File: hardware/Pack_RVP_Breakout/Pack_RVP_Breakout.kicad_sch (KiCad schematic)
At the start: 4 parts, among them Q1 Q_PMOS_GDS, Q2 Q_PMOS_GDS

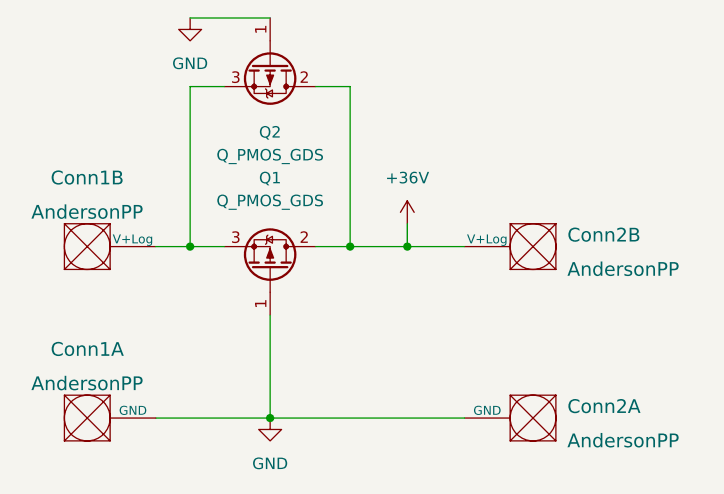
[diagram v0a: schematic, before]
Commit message: Made 30V version
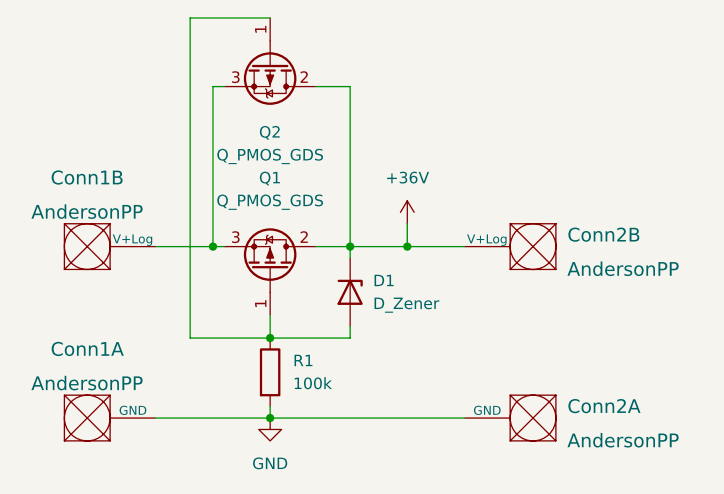
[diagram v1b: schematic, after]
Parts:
- added D1: D_Zener, MRDT_Passives:SOT-23_Diode, symbol Device:D_Zener
- added R1: 100k, Resistor_SMD:R_0603_1608Metric_Pad0.98x0.95mm_HandSolder, symbol Device:R
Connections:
- net +36V: now also D1.1 (K)
- net GND: now also R1.2; no longer Q1.1 (G), Q2.1 (G)
- new net: D1.2 (A), Q1.1 (G), Q2.1 (G), R1.1
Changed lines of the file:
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@@
   (junction (at 106.68 69.85) (diameter 0) (color 0 0 0 0)
   )
+  (junction (at 85.09 69.85) (diameter 0) (color 0 0 0 0)
+  )
   (junction (at 91.44 88.9) (diameter 0) (color 0 0 0 0)
   )
-  (junction (at 82.55 69.85) (diameter 0) (color 0 0 0 0)
-  )
   (junction (at 100.33 69.85) (diameter 0) (color 0 0 0 0)
   )
-  (wire (pts (xy 86.36 52.07) (xy 82.55 52.07))
+  (junction (at 91.44 80.01) (diameter 0) (color 0 0 0 0)
+  )
+  (wire (pts (xy 86.36 52.07) (xy 85.09 52.07))
+    (stroke (width 0) (type default) (color 0 0 0 0))
+  )
+  (wire (pts (xy 82.55 44.45) (xy 82.55 80.01))
     (stroke (width 0) (type default) (color 0 0 0 0))
   )
@@
     (stroke (width 0) (type default) (color 0 0 0 0))
   )
-  (wire (pts (xy 82.55 52.07) (xy 82.55 69.85))
-    (stroke (width 0) (type default) (color 0 0 0 0))
-  )
   (wire (pts (xy 78.74 88.9) (xy 91.44 88.9))
     (stroke (width 0) (type default) (color 0 0 0 0))
   )
+  (wire (pts (xy 85.09 52.07) (xy 85.09 69.85))
+    (stroke (width 0) (type default) (color 0 0 0 0))
+  )
   (wire (pts (xy 82.55 44.45) (xy 91.44 44.45))
     (stroke (width 0) (type default) (color 0 0 0 0))
   )
+  (wire (pts (xy 100.33 78.74) (xy 100.33 80.01))
+    (stroke (width 0) (type default) (color 0 0 0 0))
+  )
+  (wire (pts (xy 82.55 80.01) (xy 91.44 80.01))
+    (stroke (width 0) (type default) (color 0 0 0 0))
+  )
+  (wire (pts (xy 100.33 69.85) (xy 100.33 71.12))
+    (stroke (width 0) (type default) (color 0 0 0 0))
+  )
   (wire (pts (xy 106.68 69.85) (xy 113.03 69.85))
     (stroke (width 0) (type default) (color 0 0 0 0))
   )
-  (wire (pts (xy 82.55 69.85) (xy 86.36 69.85))
-    (stroke (width 0) (type default) (color 0 0 0 0))
-  )
-  (wire (pts (xy 78.74 69.85) (xy 82.55 69.85))
+  (wire (pts (xy 91.44 87.63) (xy 91.44 88.9))
+    (stroke (width 0) (type default) (color 0 0 0 0))
+  )
+  (wire (pts (xy 78.74 69.85) (xy 85.09 69.85))
     (stroke (width 0) (type default) (color 0 0 0 0))
   )
@@
     (stroke (width 0) (type default) (color 0 0 0 0))
   )
+  (wire (pts (xy 100.33 80.01) (xy 91.44 80.01))
+    (stroke (width 0) (type default) (color 0 0 0 0))
+  )
+  (wire (pts (xy 85.09 69.85) (xy 86.36 69.85))
+    (stroke (width 0) (type default) (color 0 0 0 0))
+  )
   (wire (pts (xy 96.52 69.85) (xy 100.33 69.85))
     (stroke (width 0) (type default) (color 0 0 0 0))
   )
-  (wire (pts (xy 91.44 77.47) (xy 91.44 88.9))
+  (wire (pts (xy 91.44 77.47) (xy 91.44 80.01))
     (stroke (width 0) (type default) (color 0 0 0 0))
   )
@@
     (stroke (width 0) (type default) (color 0 0 0 0))
   )
+  (symbol (lib_id "Device:R") (at 91.44 83.82 0) (unit 1)
+    (in_bom yes) (on_board yes) (fields_autoplaced)
+    (property "Reference" "R1" (id 0) (at 93.98 82.5499 0)
+      (effects (font (size 1.27 1.27)) (justify left))
+    )
+    (property "Value" "100k" (id 1) (at 93.98 85.0899 0)
+      (effects (font (size 1.27 1.27)) (justify left))
+    )
+    (property "Footprint" "Resistor_SMD:R_0603_1608Metric_Pad0.98x0.95mm_HandSolder" (id 2) (at 89.662 83.82 90)
+      (effects (font (size 1.27 1.27)) hide)
+    )
+    (property "Datasheet" "~" (id 3) (at 91.44 83.82 0)
+      (effects (font (size 1.27 1.27)) hide)
+    )
+    (pin "1")
+    (pin "2")
+  )
   (symbol (lib_id "power:+36V") (at 106.68 67.31 0) (unit 1)
     (in_bom yes) (on_board yes) (fields_autoplaced)
-    (property "Reference" "#PWR?" (id 0) (at 106.68 71.12 0)
+    (property "Reference" "#PWR03" (id 0) (at 106.68 71.12 0)
       (effects (font (size 1.27 1.27)) hide)
     )
@@
     )
     (pin "1")
+  )
+  (symbol (lib_id "Device:D_Zener") (at 100.33 74.93 270) (unit 1)
+    (in_bom yes) (on_board yes) (fields_autoplaced)
+    (property "Reference" "D1" (id 0) (at 102.87 73.6599 90)
+      (effects (font (size 1.27 1.27)) (justify left))
+    )
+    (property "Value" "D_Zener" (id 1) (at 102.87 76.1999 90)
+      (effects (font (size 1.27 1.27)) (justify left))
+    )
+    (property "Footprint" "MRDT_Passives:SOT-23_Diode" (id 2) (at 100.33 74.93 0)
+      (effects (font (size 1.27 1.27)) hide)
+    )
+    (property "Datasheet" "~" (id 3) (at 100.33 74.93 0)
+      (effects (font (size 1.27 1.27)) hide)
+    )
+    (pin "1")
+    (pin "2")
   )
   (symbol (lib_id "MRDT_Connectors:AndersonPP") (at 123.19 86.36 180) (unit 1)
@@
     (pin "3")
   )
-  (symbol (lib_id "power:GND") (at 82.55 44.45 0) (unit 1)
-    (in_bom yes) (on_board yes) (fields_autoplaced)
-    (property "Reference" "#PWR01" (id 0) (at 82.55 50.8 0)
-      (effects (font (size 1.27 1.27)) hide)
-    )
-    (property "Value" "GND" (id 1) (at 82.55 49.53 0))
-    (property "Footprint" "" (id 2) (at 82.55 44.45 0)
-      (effects (font (size 1.27 1.27)) hide)
-    )
-    (property "Datasheet" "" (id 3) (at 82.55 44.45 0)
-      (effects (font (size 1.27 1.27)) hide)
-    )
-    (pin "1")
-  )
   (symbol (lib_id "MRDT_Connectors:AndersonPP") (at 68.58 72.39 0) (unit 2)
     (in_bom yes) (on_board yes) (fields_autoplaced)
@@
   )
   (symbol_instances
-    (path "/a9c27a39-bf45-4cb5-bfa0-b90d6962e4f4"
-      (reference "#PWR01") (unit 1) (value "GND") (footprint "")
-    )
     (path "/8c1e4ba9-8831-4922-8e54-8539c3746a29"
       (reference "#PWR02") (unit 1) (value "GND") (footprint "")
     )
     (path "/225a2d45-6c6b-4a47-9d5d-9672bab3e19e"
-      (reference "#PWR?") (unit 1) (value "+36V") (footprint "")
+      (reference "#PWR03") (unit 1) (value "+36V") (footprint "")
     )
     (path "/ea49d757-a4e0-4a90-a998-1e2adfc9da37"
@@
       (reference "Conn2") (unit 2) (value "AndersonPP") (footprint "MRDT_Connectors:Square_Anderson_2_V_Side_By_Side")
     )
+    (path "/350a05c2-932c-477a-a78a-01523dbc1703"
+      (reference "D1") (unit 1) (value "D_Zener") (footprint "MRDT_Passives:SOT-23_Diode")
+    )
     (path "/a8ea599b-76cb-4fe8-8145-cef8d3f5df3c"
       (reference "Q1") (unit 1) (value "Q_PMOS_GDS") (footprint "Package_TO_SOT_SMD:TO-252-3_TabPin2")
@@
       (reference "Q2") (unit 1) (value "Q_PMOS_GDS") (footprint "Package_TO_SOT_SMD:TO-252-3_TabPin2")
     )
-  )
+    (path "/0f800890-ad14-4271-855b-fde713ed1d93"
+      (reference "R1") (unit 1) (value "100k") (footprint "Resistor_SMD:R_0603_1608Metric_Pad0.98x0.95mm_HandSolder")
+    )
+  )
